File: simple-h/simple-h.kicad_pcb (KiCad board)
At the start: 2 copper layers, 57.2 x 63.5 mm, 35 parts, among them J1 Conn_02x04_Odd_Even, J2 CN1, J3 FAN, J4 M1, J5 M2, J6 B+, J7 B-, Q1 BTS7960B, Q2 BTS7960B

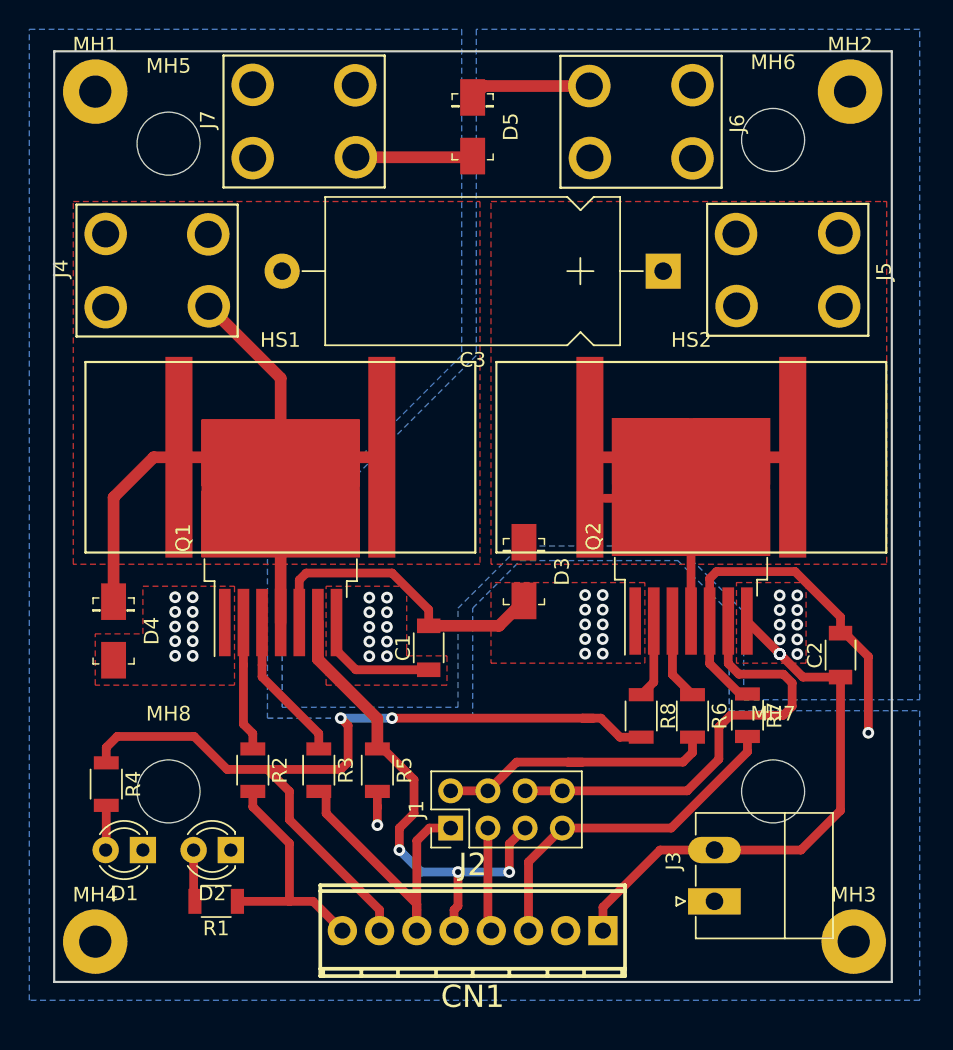
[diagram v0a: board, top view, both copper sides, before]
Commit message: Se agregaron modelos 3D
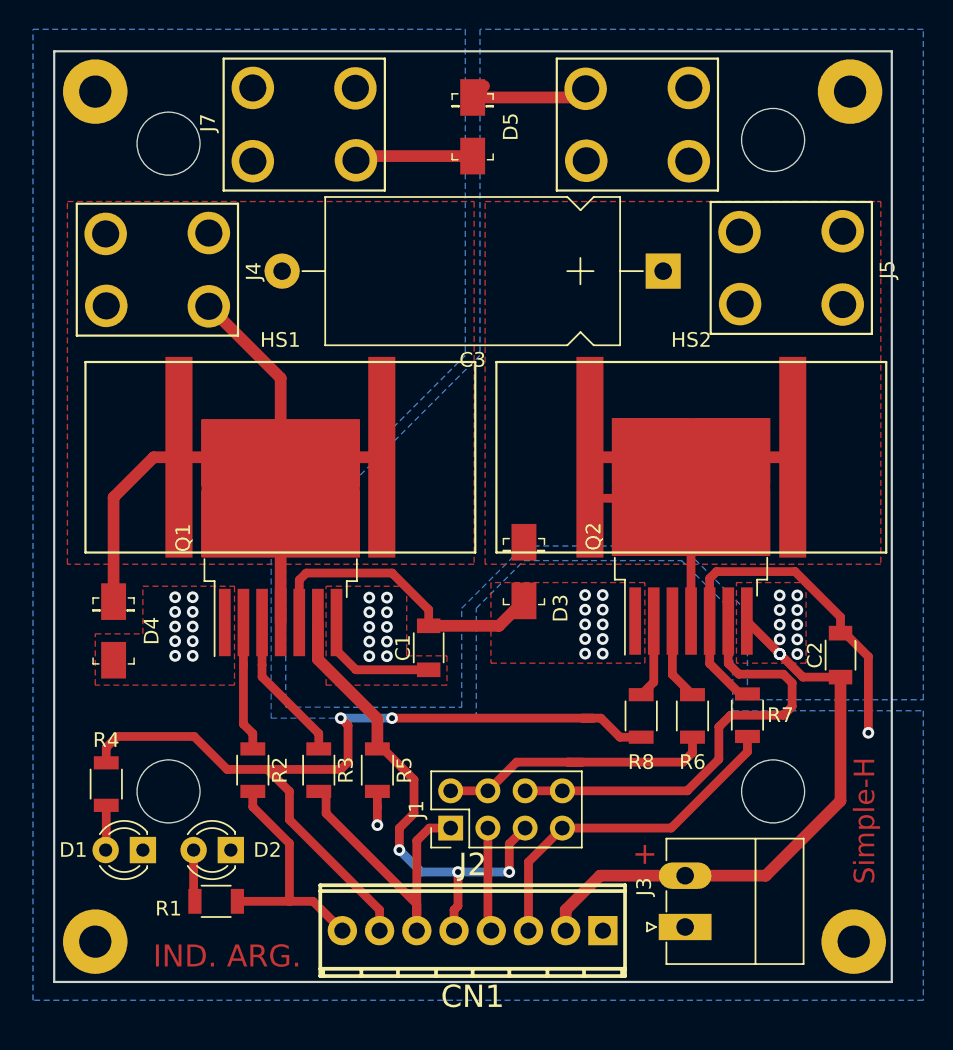
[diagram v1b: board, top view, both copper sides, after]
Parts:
- moved J4 8.54 mm to (135.0, 50.9), turned to 90 degrees
- moved J3 2.66 mm to (174.5, 93.2)
- moved J6 0.31 mm to (167.7, 41.0)
- moved J5 0.27 mm to (178.2, 50.8)
- moved J7 0.21 mm to (152.0, 36.0)
- renumbered MH4 to ?
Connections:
- J2 pad 1: VDD -> GND
- J2 pad 2: GND -> VDD
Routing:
- net VDD: track 55.5 -> 57.5 mm
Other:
- board text added: "+"
- board text added: "B+"
- board text added: "B-"
- board text added: "IND. ARG."
- board text added: "Simple-H"

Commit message: Se agregaron los modelos 3D al proyecto
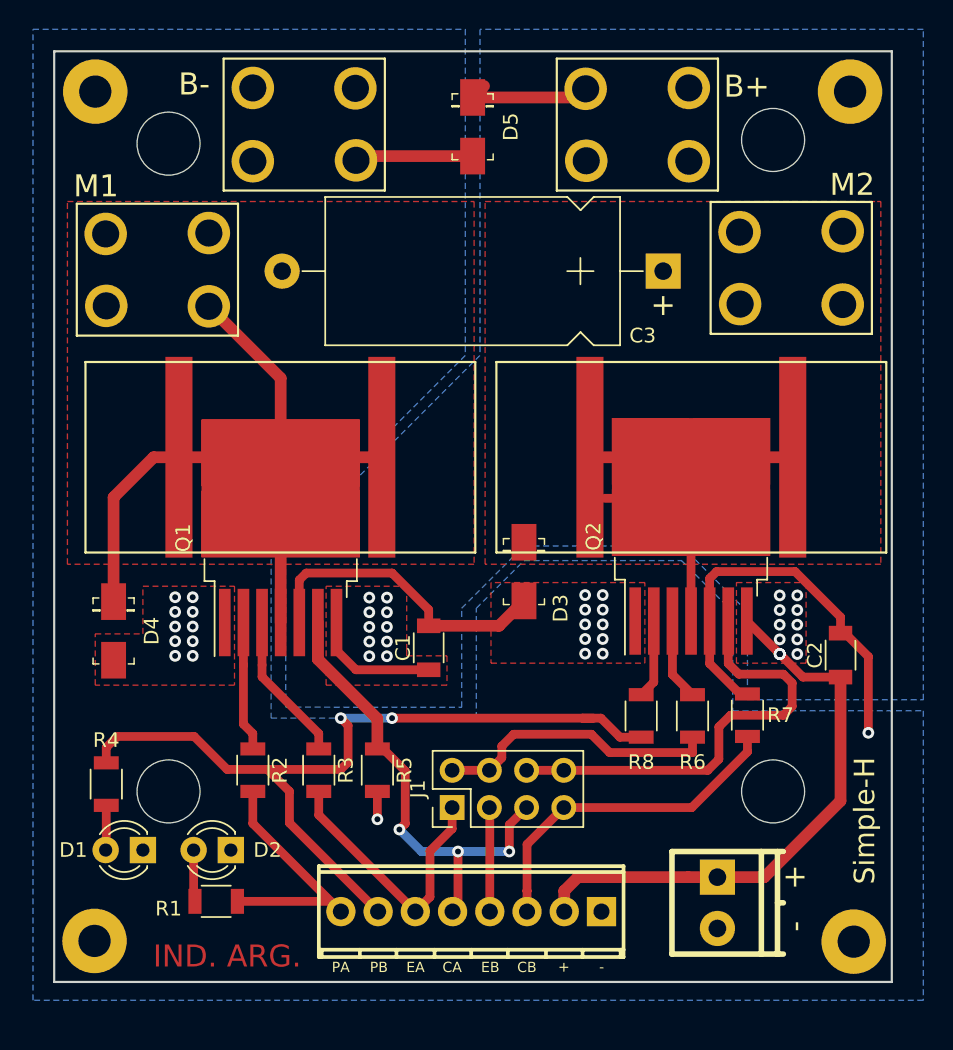
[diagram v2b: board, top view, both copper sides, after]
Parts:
- removed ?: MountingHole, Mounting_Holes:MountingHole_2.2mm_M2_Pad
- added MH4: MountingHole, Mounting_Holes:MountingHole_2.2mm_M2_Pad, F.Cu at (134.2, 94.2)
- J3: footprint Connectors_Phoenix:PhoenixContact_MC-G_02x3.50mm_Angled -> w_conn_pt-1,5:pt_1,5-2-3,5-h
- moved J3 3.34 mm to (177.4, 91.6)
- moved J1 1.40 mm to (158.6, 85.1)
- moved J2 1.30 mm to (159.9, 92.2)
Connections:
- J3 pad 1: GND -> VDD
- J3 pad 2: VDD -> GND
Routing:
- net /EN-A: track 21.0 -> 19.1 mm
- net /PWM-A: track 16.5 -> 18.0 mm
- net /PWM-B: track 58.6 -> 57.2 mm
- net /CURR-A: track 34.6 -> 33.2 mm
- net Net-(J1-Pad6): track 31.3 -> 30.6 mm
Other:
- board text added: "-"
- board text added: "CA"
- board text added: "CB"
- board text added: "EA"
- board text added: "EB"
- board text added: "M1"
- board text added: "M2"
- board text added: "PA"
- board text added: "PB"

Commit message: Se agregaron comentarios
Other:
- board text added: "Mínimos (Mayer 10 mils): Grillas: 1mm, 0.5mm Vía: 0.8mm Margen: 0.25mm Pista: 0.6mm, 0.8mm Dist. a borde: 0.3mm Terminación: HASL"
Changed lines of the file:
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@@
   (general
     (thickness 1.6)
-    (drawings 22)
+    (drawings 26)
     (tracks 196)
     (zones 0)
@@
       (effects (font (size 1 1) (thickness 0.15)))
     )
-    (fp_text value Heatsink_Pad (at 0 8) (layer F.Fab)
+    (fp_text value Heatsink_Pad (at 0 8) (layer F.Fab) hide
       (effects (font (size 1 1) (thickness 0.15)))
     )
@@
       (effects (font (size 1 1) (thickness 0.15)))
     )
-    (fp_text value Heatsink_Pad (at 0 8) (layer F.Fab)
+    (fp_text value Heatsink_Pad (at 0 8) (layer F.Fab) hide
       (effects (font (size 1 1) (thickness 0.15)))
     )
@@
     )
   )
+  (gr_text "Mínimos (Mayer 10 mils):\nGrillas: 1mm, 0.5mm\nVía: 0.8mm\nMargen: 0.25mm\nPista: 0.6mm, 0.8mm\nDist. a borde: 0.3mm\nTerminación: HASL" (at 206.73 65.1) (layer Dwgs.User)
+    (effects (font (size 1.5 1.5) (thickness 0.3)) (justify left))
+  )
+  (dimension 63.5 (width 0.3) (layer Dwgs.User)
+    (gr_text "63.500 mm" (at 199.79 65.26 270) (layer Dwgs.User)
+      (effects (font (size 1.5 1.5) (thickness 0.3)))
+    )
+    (feature1 (pts (xy 188.59 97.01) (xy 198.276421 97.01)))
+    (feature2 (pts (xy 188.59 33.51) (xy 198.276421 33.51)))
+    (crossbar (pts (xy 197.69 33.51) (xy 197.69 97.01)))
+    (arrow1a (pts (xy 197.69 97.01) (xy 197.103579 95.883496)))
+    (arrow1b (pts (xy 197.69 97.01) (xy 198.276421 95.883496)))
+    (arrow2a (pts (xy 197.69 33.51) (xy 197.103579 34.636504)))
+    (arrow2b (pts (xy 197.69 33.51) (xy 198.276421 34.636504)))
+  )
+  (dimension 2.760289 (width 0.1) (layer Dwgs.User)
+    (gr_text "3.175 mm" (at 125.63 34.889855 90) (layer Dwgs.User)
+      (effects (font (size 1.5 1.5) (thickness 0.1)))
+    )
+    (feature1 (pts (xy 134.28 33.509711) (xy 127.143579 33.509711)))
+    (feature2 (pts (xy 134.28 36.27) (xy 127.143579 36.27)))
+    (crossbar (pts (xy 127.73 36.27) (xy 127.73 33.509711)))
+    (arrow1a (pts (xy 127.73 33.509711) (xy 128.316421 34.636215)))
+    (arrow1b (pts (xy 127.73 33.509711) (xy 127.143579 34.636215)))
+    (arrow2a (pts (xy 127.73 36.27) (xy 128.316421 35.143496)))
+    (arrow2b (pts (xy 127.73 36.27) (xy 127.143579 35.143496)))
+  )
+  (dimension 57.144337 (width 0.1) (layer Dwgs.User)
+    (gr_text "57.15 mm" (at 160.032168 22.53) (layer Dwgs.User)
+      (effects (font (size 1.5 1.5) (thickness 0.1)))
+    )
+    (feature1 (pts (xy 188.604337 33.5) (xy 188.604337 24.043579)))
+    (feature2 (pts (xy 131.46 33.5) (xy 131.46 24.043579)))
+    (crossbar (pts (xy 131.46 24.63) (xy 188.604337 24.63)))
+    (arrow1a (pts (xy 188.604337 24.63) (xy 187.477833 25.216421)))
+    (arrow1b (pts (xy 188.604337 24.63) (xy 187.477833 24.043579)))
+    (arrow2a (pts (xy 131.46 24.63) (xy 132.586504 25.216421)))
+    (arrow2b (pts (xy 131.46 24.63) (xy 132.586504 24.043579)))
+  )
   (gr_text M2 (at 185.9 42.6) (layer F.SilkS)
